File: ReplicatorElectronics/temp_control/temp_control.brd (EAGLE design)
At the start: 44.5 x 42.2 mm, 4 parts, among them Q1 IRL640A

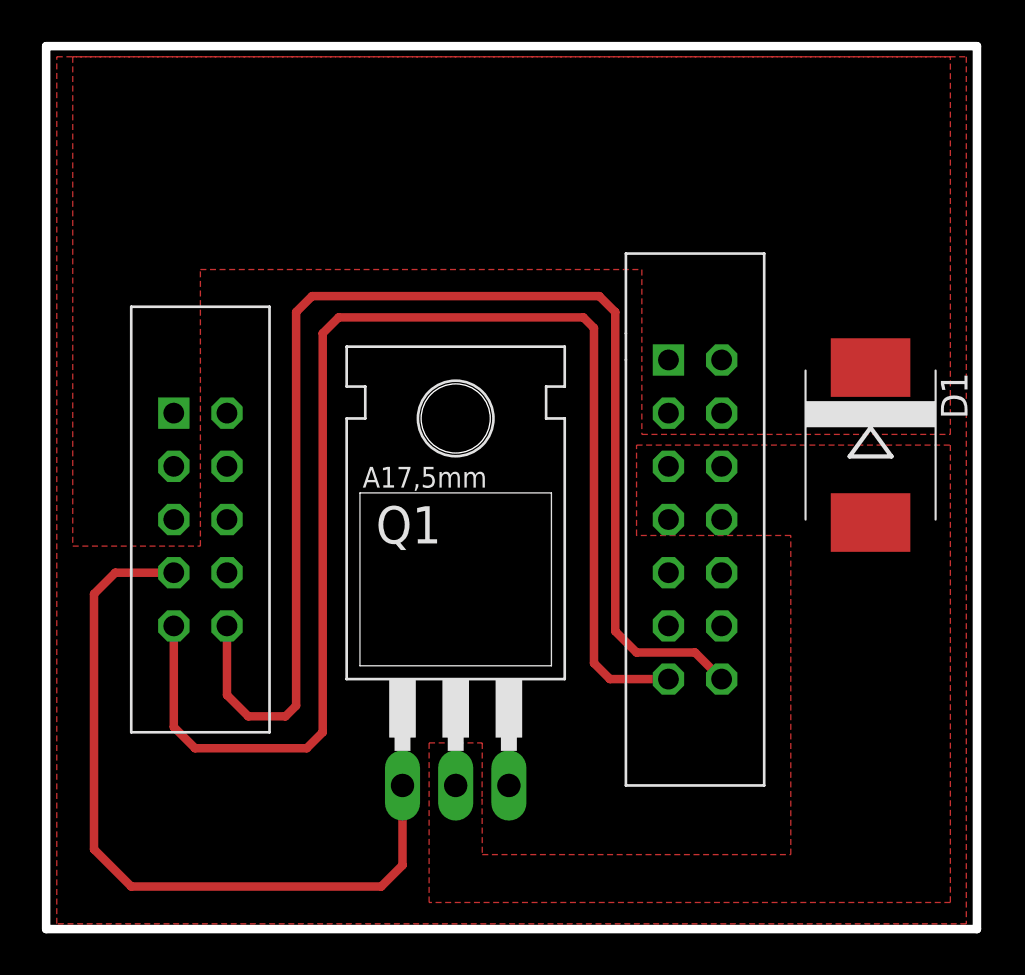
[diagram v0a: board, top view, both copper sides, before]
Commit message: 3/17/12: Rev. 02 Temp Control Board. Replaced 2x7 rectangular header with 0.100" pitch screw terminal, added high-side totem pole driver for MOSFET, added clearance holes for mounting screws. Swapped diode D1 for slightly smaller part.
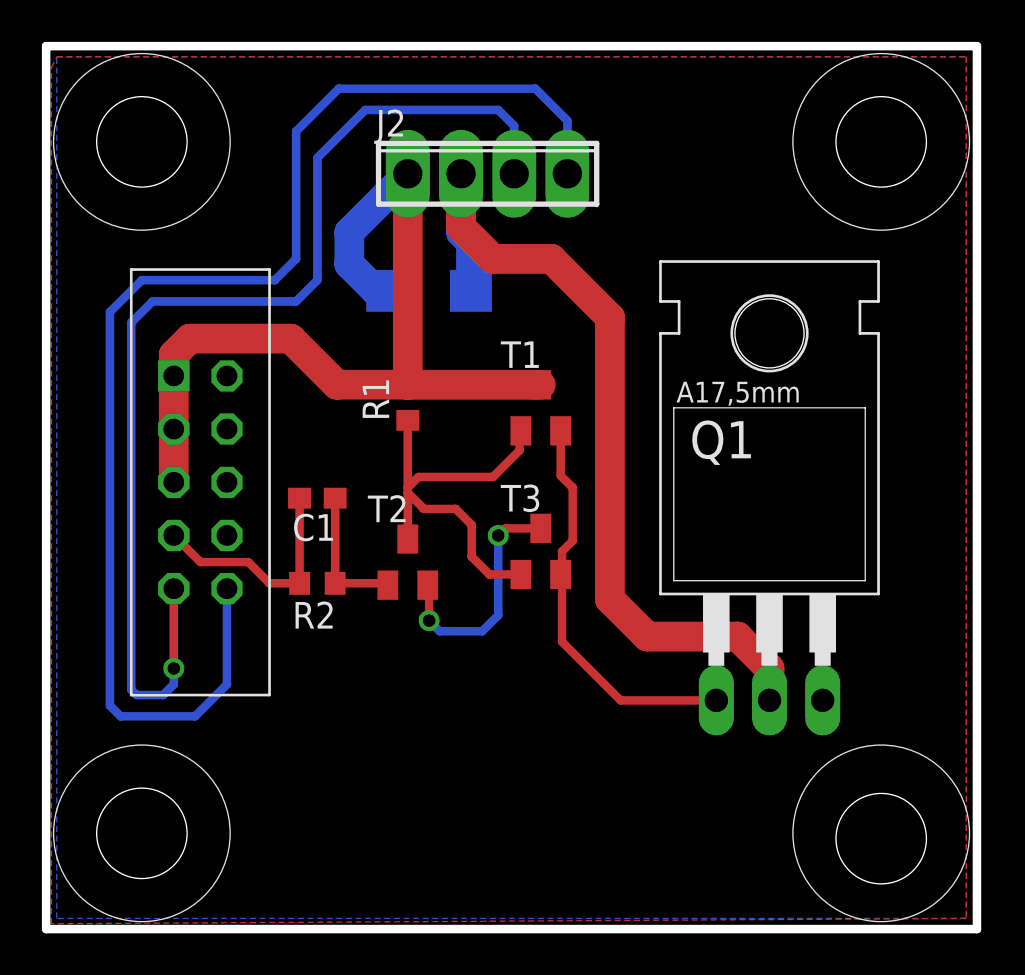
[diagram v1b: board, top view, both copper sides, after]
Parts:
- removed U$1: SBH11-PBPC-D05-ST-BK, SBH11-PBPC-D05-ST-BK:SBH11-PBPC-D05-ST-BK
- removed U$2: SBH11-PBPC-D07-ST-BK, SBH11-PBPC-D07-ST-BK:SBH11-PBPC-D07-ST-BK
- added C1: 0.1uF, resistor:C0603
- added J1: SBH11-PBPC-D05-ST-BK, SBH11-PBPC-D05-ST-BK:SBH11-PBPC-D05-ST-BK
- added J2: OSTVN04A150, con-OST-254:4POL254
- added R1: 8.2k, resistor:R0603
- added R2: 4.7k, resistor:R0603
- added T1, T2: MMBT2222A, transistor:SOT23-BEC
- added T3: MMBT3906LT1, transistor:SOT23-BEC
- D1: value S8KC-13 -> B340A-13-F; device diode:SMC -> chipKIT_Max32:DISCRETE_SMA
- moved D1 22.3 mm to (18.3, 30.7), flipped to the bottom, turned to 180 degrees
- moved Q1 15.5 mm to (34.5, 17.5)
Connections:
- new net N$3: C1.1, R2.1, T2.B
- new net N$4: R1.1, T1.B, T2.C, T3.B
- new net N$6: Q1.1, T1.E, T3.E
- new net N$8: T2.E, T3.C
- net CTRL: now also C1.2, J1.7, R2.2; no longer Q1.1, U$1.7
- net GND: now also J1.2, J1.4, J1.6, J1.8; no longer U$1.2, U$1.4, U$1.6, U$1.8
- net HEAT0: now also J2.2; no longer U$2.5, U$2.6, U$2.7, U$2.8
- net THERM1: now also J1.9, J2.3; no longer U$1.9, U$2.13
- net THERM2: now also J1.10, J2.4; no longer U$1.10, U$2.14
- net VCC: now also J1.1, J1.3, J1.5, J2.1, R1.2, T1.C; no longer U$1.1, U$1.3, U$1.5, U$2.1, U$2.2, U$2.3, U$2.4
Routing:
- net VCC: track 0.00 -> 42.7 mm
- net HEAT0: track 0.00 -> 41.2 mm
- net CTRL: track 36.1 -> 11.2 mm
- net N$4: track 0.00 -> 20.4 mm
- net N$6: track 0.00 -> 19.1 mm
- net THERM1: track 65.1 -> 53.0 mm, vias 0 -> 1
- net N$8: track 0.00 -> 11.5 mm, vias 0 -> 2
- net N$3: track 0.00 -> 6.77 mm
- added copper zone on layer 16, net GND
- removed copper zone on layer 1, net HEAT0
- removed copper zone on layer 1, net VCC

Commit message: 3/31/12: Rev. 3 of temp control board. Modified 2x5 header symbol, generated DXF files (one with holes only, another with holes and high-profile parts).
~ 0.5 hrs invested.
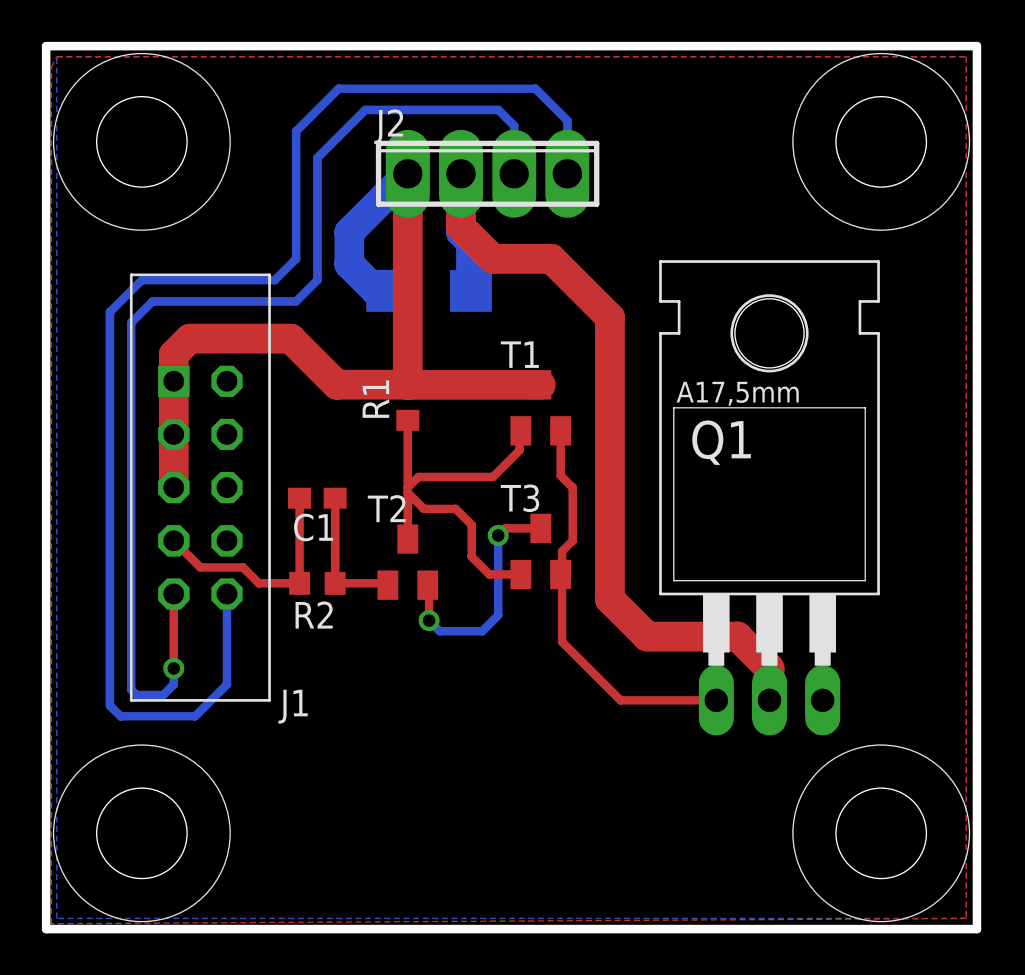
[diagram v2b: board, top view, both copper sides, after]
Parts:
- Q1: value IRL640A -> IRL540N
- moved J1 0.25 mm to (6.10, 26.4)
